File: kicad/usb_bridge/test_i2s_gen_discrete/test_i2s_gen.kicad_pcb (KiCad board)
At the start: 2 copper layers, 40 x 40 mm, 26 parts, among them J1 Conn_01x02_Male, J2 Conn_01x04_Male, U1 74ALVC14, U2 74AHC86, U3 74HC4020, U4 74AHC595, U5 74AHC595, Y1 Crystal

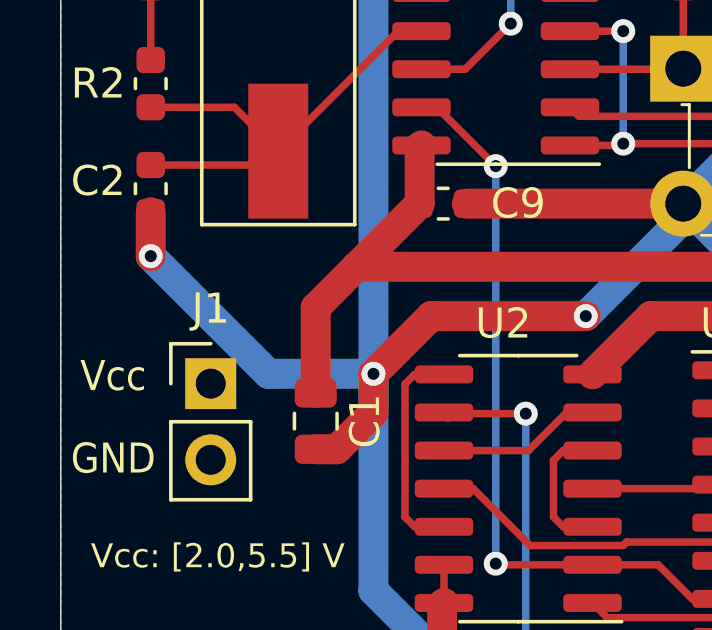
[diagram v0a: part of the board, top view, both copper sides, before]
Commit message: I2S test generator refinements
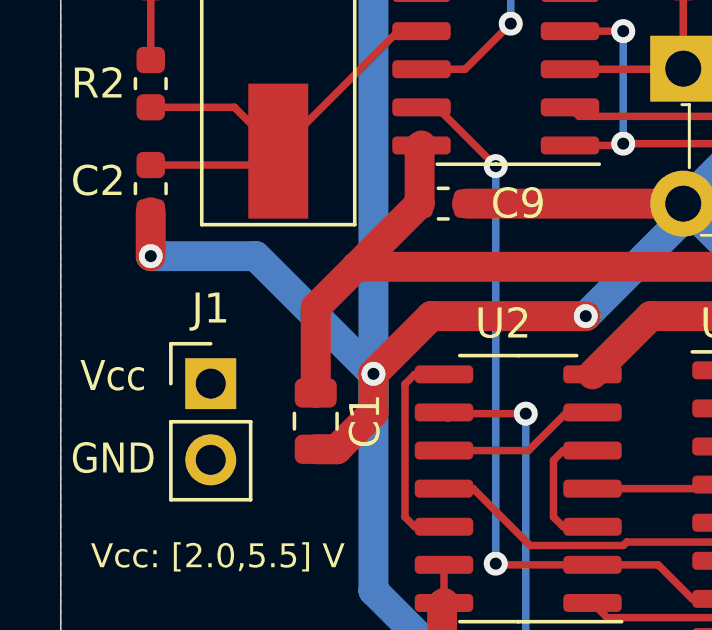
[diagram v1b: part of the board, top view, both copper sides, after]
